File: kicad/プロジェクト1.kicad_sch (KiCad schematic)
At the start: 8 parts, among them J1 Barrel_Jack_Switch_Pin3Ring, Q1 2SC1815, Q2 2SA1015

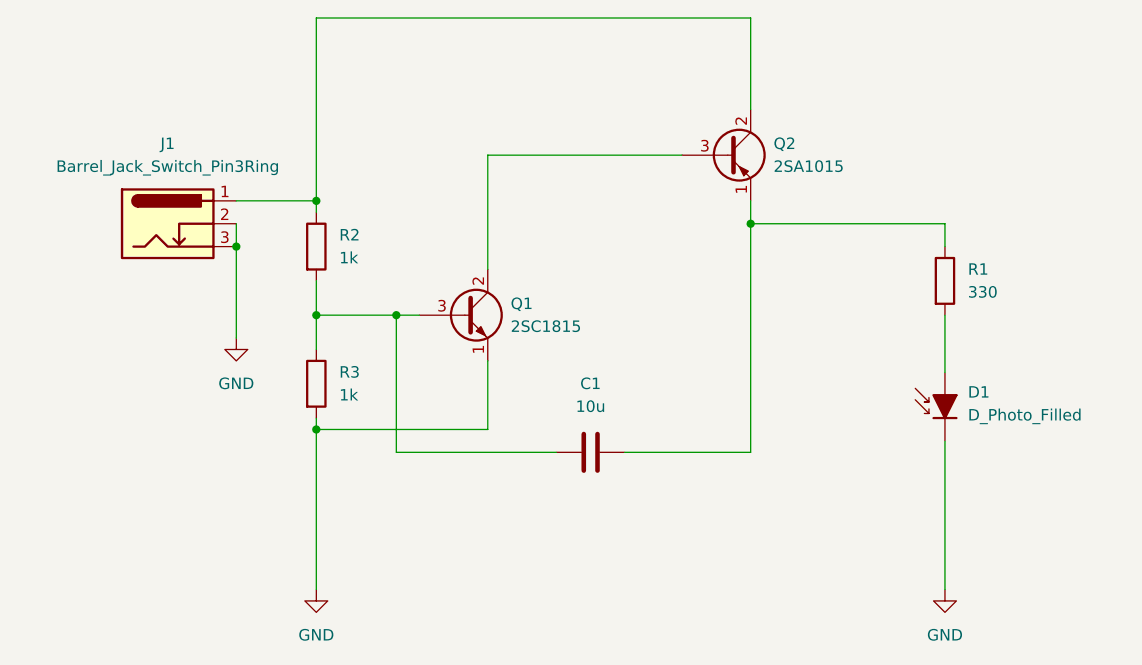
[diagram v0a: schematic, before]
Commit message: 回路図を修正
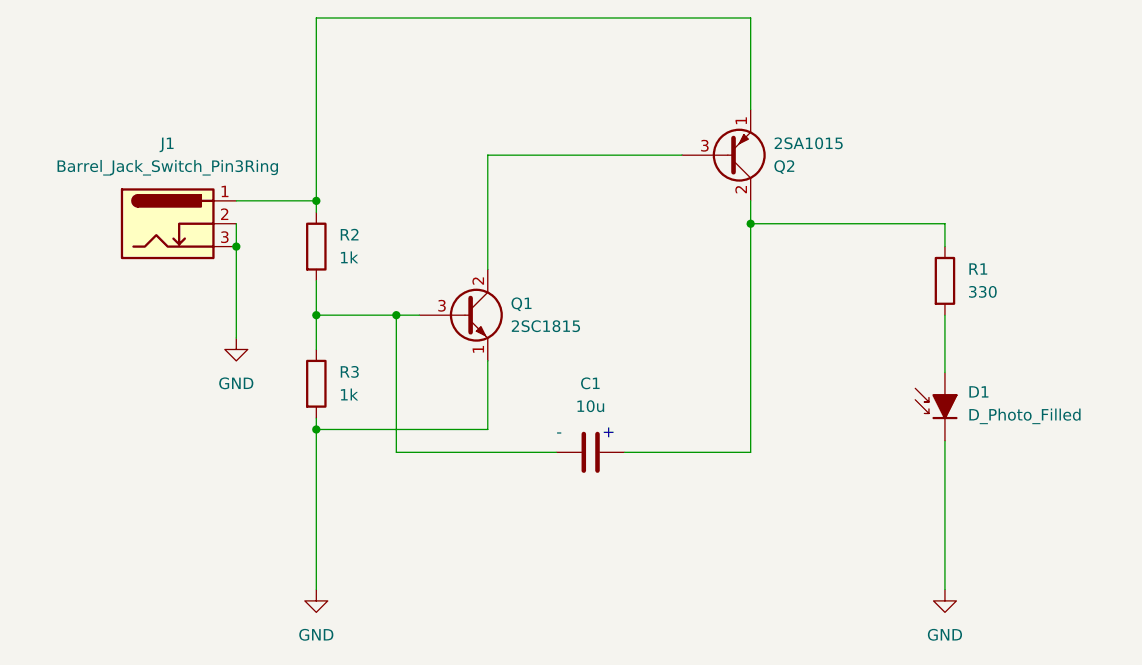
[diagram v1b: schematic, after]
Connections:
- net at J1.1, R2.1: now also Q2.1 (E); no longer Q2.2 (C)
- net at Q1.3 (B), R2.2, R3.1: now also C1.2; no longer C1.1
- new net: C1.1, Q2.2 (C), R1.1
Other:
- note added: "+"
- note added: "-"
- moved on the sheet: C1
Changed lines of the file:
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@@
   (junction (at 116.84 107.95) (diameter 0) (color 0 0 0 0)
+  )
+  (junction (at 165.1 85.09) (diameter 0) (color 0 0 0 0)
   )
   (junction (at 116.84 82.55) (diameter 0) (color 0 0 0 0)
   )
   (junction (at 107.95 87.63) (diameter 0) (color 0 0 0 0)
-  )
-  (junction (at 165.1 85.09) (diameter 0) (color 0 0 0 0)
   )
   (junction (at 116.84 95.25) (diameter 0) (color 0 0 0 0)
@@
     (stroke (width 0) (type default))
   )
-  (wire (pts (xy 165.1 85.09) (xy 165.1 82.55))
+  (wire (pts (xy 125.73 95.25) (xy 128.27 95.25))
     (stroke (width 0) (type default))
   )
-  (wire (pts (xy 125.73 95.25) (xy 128.27 95.25))
+  (wire (pts (xy 186.69 109.22) (xy 186.69 125.73))
     (stroke (width 0) (type default))
   )
@@
     (stroke (width 0) (type default))
   )
-  (wire (pts (xy 186.69 109.22) (xy 186.69 125.73))
-    (stroke (width 0) (type default))
-  )
   (wire (pts (xy 107.95 82.55) (xy 116.84 82.55))
     (stroke (width 0) (type default))
   )
   (wire (pts (xy 165.1 62.23) (xy 116.84 62.23))
+    (stroke (width 0) (type default))
+  )
+  (wire (pts (xy 165.1 82.55) (xy 165.1 85.09))
     (stroke (width 0) (type default))
   )
@@
     (stroke (width 0) (type default))
   )
-  (symbol (lib_id "Transistor_BJT:2SA1015") (at 162.56 77.47 0) (unit 1)
-    (in_bom yes) (on_board yes) (dnp no) (fields_autoplaced)
-    (property "Reference" "Q2" (at 167.64 76.2 0)
+  (text "-" (at 143.51 109.22 0)
+    (effects (font (size 1.27 1.27)) (justify left bottom))
+  )
+  (text "+" (at 148.59 109.22 0)
+    (effects (font (size 1.27 1.27)) (justify left bottom))
+  )
+  (symbol (lib_id "Transistor_BJT:2SA1015") (at 162.56 77.47 0) (mirror x) (unit 1)
+    (in_bom yes) (on_board yes) (dnp no)
+    (property "Reference" "Q2" (at 167.64 78.74 0)
       (effects (font (size 1.27 1.27)) (justify left))
     )
-    (property "Value" "2SA1015" (at 167.64 78.74 0)
+    (property "Value" "2SA1015" (at 167.64 76.2 0)
       (effects (font (size 1.27 1.27)) (justify left))
     )
-    (property "Footprint" "Package_TO_SOT_THT:TO-92_Inline" (at 167.64 79.375 0)
+    (property "Footprint" "Package_TO_SOT_THT:TO-92_Inline" (at 167.64 75.565 0)
       (effects (font (size 1.27 1.27) italic) (justify left) hide)
     )
@@
     )
   )
-  (symbol (lib_id "Device:C") (at 147.32 110.49 90) (unit 1)
-    (in_bom yes) (on_board yes) (dnp no) (fields_autoplaced)
+  (symbol (lib_id "Device:C") (at 147.32 110.49 270) (mirror x) (unit 1)
+    (in_bom yes) (on_board yes) (dnp no)
     (property "Reference" "C1" (at 147.32 102.87 90)
       (effects (font (size 1.27 1.27)))
@@
       (effects (font (size 1.27 1.27)))
     )
-    (property "Footprint" "Capacitor_THT:CP_Radial_Tantal_D6.0mm_P5.00mm" (at 151.13 109.5248 0)
+    (property "Footprint" "Capacitor_THT:CP_Radial_Tantal_D6.0mm_P5.00mm" (at 143.51 109.5248 0)
       (effects (font (size 1.27 1.27)) hide)
     )
